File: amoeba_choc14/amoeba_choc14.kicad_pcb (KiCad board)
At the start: 2 copper layers, 13.7 x 16 mm, 9 parts, among them J1 Conn_01x01_Pin, J2 Conn_01x01_Pin, J3 Conn_01x01_Pin, J4 Conn_01x01_Pin, J5 Conn_01x01_Pin, SW1 SW_SPST

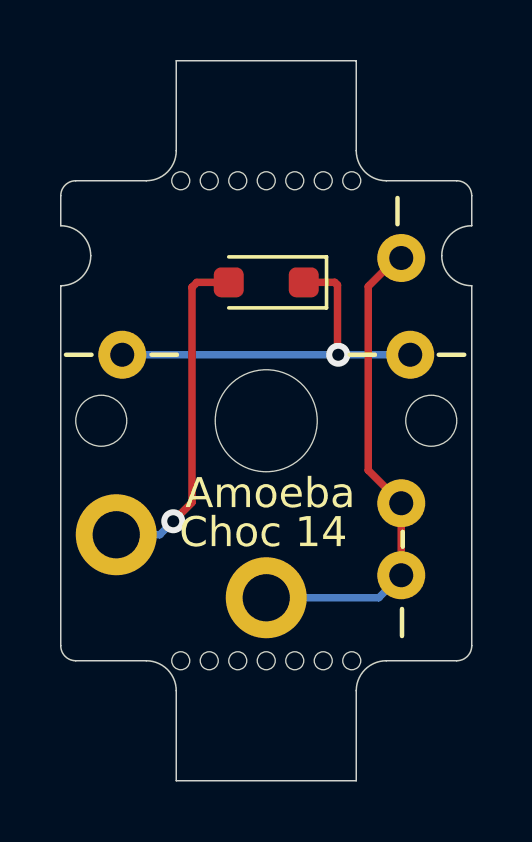
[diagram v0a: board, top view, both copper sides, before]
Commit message: feat: oval wire pads offset for easier curve
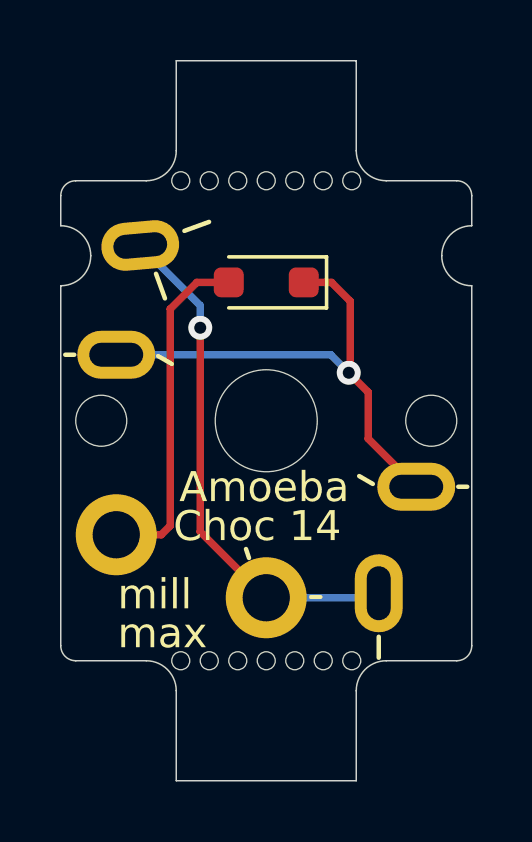
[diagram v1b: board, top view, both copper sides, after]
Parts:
- removed J5: Conn_01x01_Pin, Amoeba_Choc_Nar:Pin_D0.8mm_L7.0mm
- moved J1 8.71 mm to (125.8, 104.2), turned to -85 degrees
- moved J4 4.40 mm to (135.0, 112.2), turned to -90 degrees
- moved J2 0.96 mm to (133.8, 115.8)
- moved J3 0.20 mm to (125.0, 107.8), turned to -90 degrees
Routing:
- net /row: track 13.1 -> 16.7 mm
- net /col: track 16.3 -> 17.3 mm, vias 0 -> 1
- net Net-(D1-A): track 11.4 -> 11.5 mm, vias 1 -> 0
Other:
- board text added: "v010a2"
- board text removed: "v010a1"

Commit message: feat(pcb): use slots for wire holes. better bites
- Row and col are slots to more easily cram wire into them.
- No extra lower column pad
- Better separation between upper col and row
- Mouse bites recessed so broken edge should lie inside the board outline.
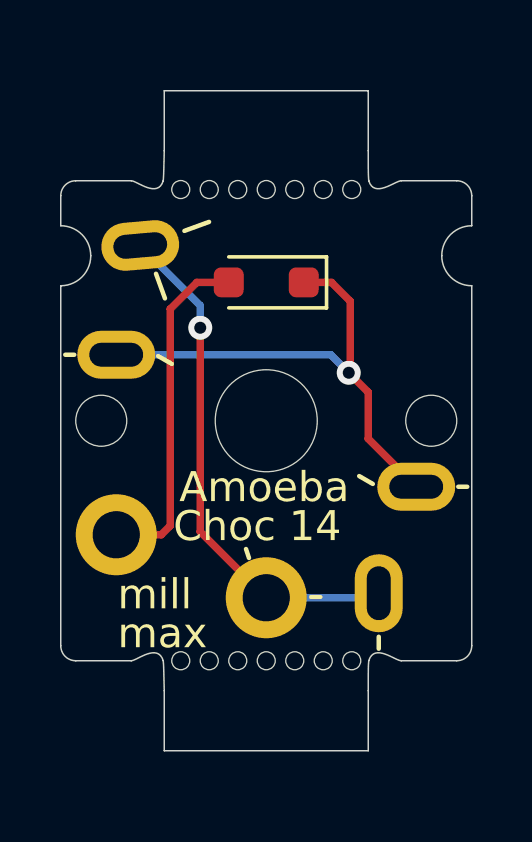
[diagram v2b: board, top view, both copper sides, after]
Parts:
- moved REF** 0.29 mm to (130.0, 102.3)
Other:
- outline, holes or cut-outs redrawn
- board text added: "Outer ticks: choc spacing - 18 x 17 Inner ticks: clip width x body length - 14.5 x 13.8 Blue outline: switch lower body - 13.8 x 13.8"
- board text added: "clip area"
- board text removed: "Outer ticks are choc spacing, 18 x 17 Inner ticks are clip width x body depth, 14.5 x 13.8 Blue outline is switch lower body, 13.8 x 13.8"
